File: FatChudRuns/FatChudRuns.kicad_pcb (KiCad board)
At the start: 2 copper layers, 0 parts

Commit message: selected rj45 w/ mag, fixed filtering for power, added snippets of layout recs
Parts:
- added J1: RJ45_Pulse_JXD6-0001NL, Connector_RJ:RJ45_Pulse_JXD6-0001NL_Horizontal, F.Cu at (-41.8, 67.0)
- added R1: 4.7k, Resistor_SMD:R_0603_1608Metric, F.Cu at (-10.6, 58.8)
- added R10: 2.2k, Resistor_SMD:R_0603_1608Metric, F.Cu at (-54.4, 90.2)
- added R11: 2.2k, Resistor_SMD:R_0603_1608Metric, F.Cu at (-54.4, 92.7)
- added R12: 2.2k, Resistor_SMD:R_0603_1608Metric, F.Cu at (-54.4, 95.2)
- added R13: 2.2k, Resistor_SMD:R_0603_1608Metric, F.Cu at (-54.4, 97.7)
- added R14: 2.2k, Resistor_SMD:R_0603_1608Metric, F.Cu at (-50.4, 77.7)
- added R15: 2.2k, Resistor_SMD:R_0603_1608Metric, F.Cu at (-50.4, 80.2)
- added R16: 2.2k, Resistor_SMD:R_0603_1608Metric, F.Cu at (-50.4, 82.7)
- added R17: 2.2k, Resistor_SMD:R_0603_1608Metric, F.Cu at (-50.4, 85.2)
- added R18: 2.2k, Resistor_SMD:R_0603_1608Metric, F.Cu at (-50.4, 87.7)
- added R19: 2.2k, Resistor_SMD:R_0603_1608Metric, F.Cu at (-50.4, 90.2)
- added R2: 4.7k, Resistor_SMD:R_0603_1608Metric, F.Cu at (-10.6, 61.3)
- added R20: 2.2k, Resistor_SMD:R_0603_1608Metric, F.Cu at (-50.4, 92.7)
- added R21: 2.2k, Resistor_SMD:R_0603_1608Metric, F.Cu at (-50.4, 95.2)
- added R22: 50, Resistor_SMD:R_0603_1608Metric, F.Cu at (-50.4, 97.7)
- added R23: 50, Resistor_SMD:R_0603_1608Metric, F.Cu at (-46.4, 77.7)
- added R24: 2.2k, Resistor_SMD:R_0603_1608Metric, F.Cu at (-46.4, 80.2)
- added R25: 50, Resistor_SMD:R_0603_1608Metric, F.Cu at (-46.4, 82.7)
- added R26: 50, Resistor_SMD:R_0603_1608Metric, F.Cu at (-46.4, 85.2)
- added R27: 2.2k, Resistor_SMD:R_0603_1608Metric, F.Cu at (-46.4, 87.7)
- added R28: 2.2k, Resistor_SMD:R_0603_1608Metric, F.Cu at (-46.4, 90.2)
- added R29: 2.2k, Resistor_SMD:R_0603_1608Metric, F.Cu at (-46.4, 92.7)
- added R3: 4.7k, Resistor_SMD:R_0603_1608Metric, F.Cu at (-10.6, 63.8)
- added R30: 2.2k, Resistor_SMD:R_0603_1608Metric, F.Cu at (-46.4, 95.2)
- added R31: 50, Resistor_SMD:R_0603_1608Metric, F.Cu at (-46.4, 97.7)
- added R32: 50, Resistor_SMD:R_0603_1608Metric, F.Cu at (-42.4, 77.7)
- added R33: 50, Resistor_SMD:R_0603_1608Metric, F.Cu at (-42.4, 80.2)
- added R34: 50, Resistor_SMD:R_0603_1608Metric, F.Cu at (-42.4, 82.7)
- added R35: 4.87k, Resistor_SMD:R_0603_1608Metric, F.Cu at (-42.4, 85.2)
- added R36: 2.2k, Resistor_SMD:R_0603_1608Metric, F.Cu at (-42.4, 87.7)
- added R37: 2.2k, Resistor_SMD:R_0603_1608Metric, F.Cu at (-42.4, 90.2)
- added R4: 4.7k, Resistor_SMD:R_0603_1608Metric, F.Cu at (-10.6, 66.3)
- added R5: 1.5k, Resistor_SMD:R_0603_1608Metric, F.Cu at (-54.4, 77.7)
- added R6: 2.2k, Resistor_SMD:R_0603_1608Metric, F.Cu at (-54.4, 80.2)
- added R7: 2.2k, Resistor_SMD:R_0603_1608Metric, F.Cu at (-54.4, 82.7)
- added R8: 0, Resistor_SMD:R_0603_1608Metric, F.Cu at (-54.4, 85.2)
- added R9: 0, Resistor_SMD:R_0603_1608Metric, F.Cu at (-54.4, 87.7)
- added U1: STM32F107RBTx, Package_QFP:LQFP-64_10x10mm_P0.5mm, F.Cu at (-19.8, 64.8)
- added U2: DP83848I, Package_QFP:LQFP-48_7x7mm_P0.5mm, F.Cu at (-34.7, 82.1)

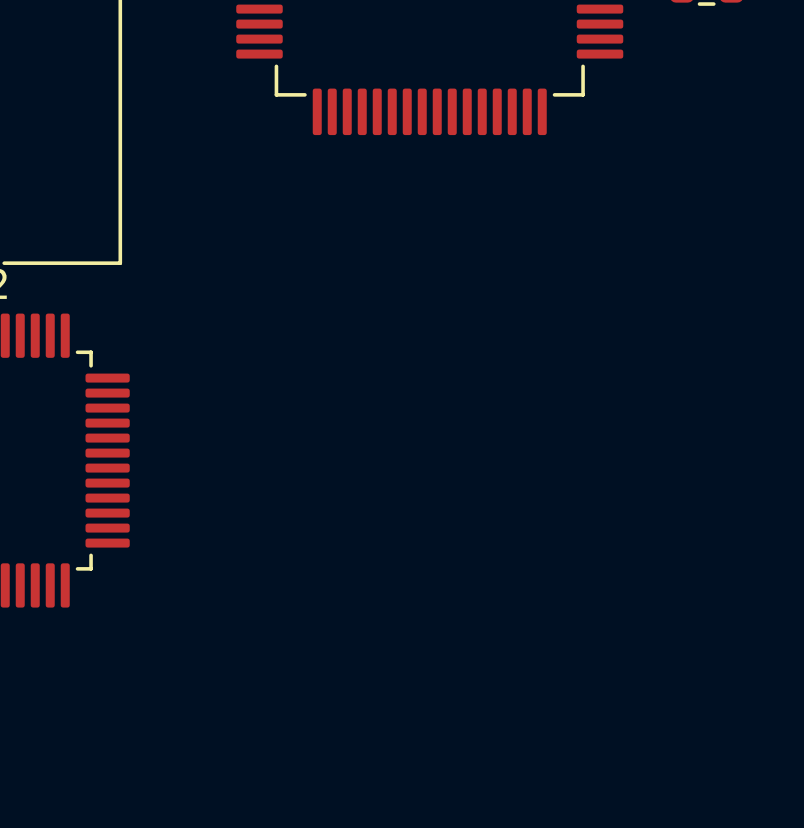
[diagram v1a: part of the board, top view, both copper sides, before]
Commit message: connected rj45 and leds and led strapping resistors
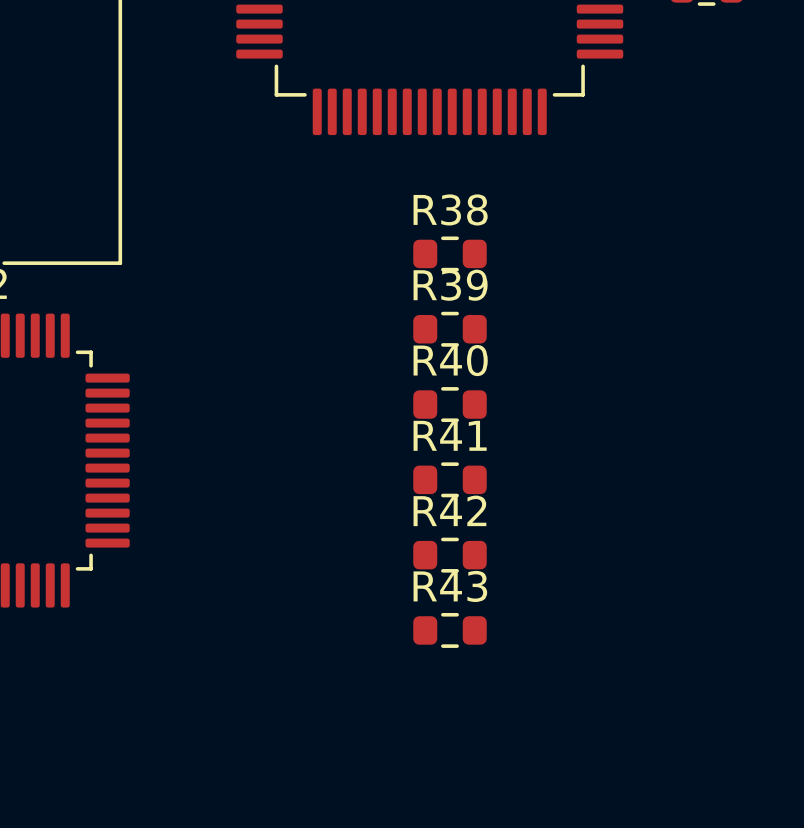
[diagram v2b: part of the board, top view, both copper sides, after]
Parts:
- added R38: 2.2k, Resistor_SMD:R_0603_1608Metric, F.Cu at (-19.2, 75.2)
- added R39: 110, Resistor_SMD:R_0603_1608Metric, F.Cu at (-19.2, 77.7)
- added R40: 2.2k, Resistor_SMD:R_0603_1608Metric, F.Cu at (-19.2, 80.2)
- added R41: 2.2k, Resistor_SMD:R_0603_1608Metric, F.Cu at (-19.2, 82.7)
- added R42: 2.2k, Resistor_SMD:R_0603_1608Metric, F.Cu at (-19.2, 85.2)
- added R43: 2.2k, Resistor_SMD:R_0603_1608Metric, F.Cu at (-19.2, 87.7)
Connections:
- J1 pad 1: unconnected-(J1-Pad1) -> /ETH_PHY/LED_LINK
- J1 pad 10: unconnected-(J1-Pad10) -> Net-(J1-Pad10)
- J1 pad 2: unconnected-(J1-Pad2) -> Net-(J1-Pad2)
- J1 pad 3: unconnected-(J1-TCT-Pad3) -> VP3V3
- J1 pad 4: unconnected-(J1-TD+-Pad4) -> /ETH_PHY/TD_P
- J1 pad 5: unconnected-(J1-TD--Pad5) -> /ETH_PHY/TD_N
- J1 pad 6: unconnected-(J1-RD+-Pad6) -> /ETH_PHY/RD_P
- J1 pad 7: unconnected-(J1-RD--Pad7) -> /ETH_PHY/RD_N
- J1 pad 8: unconnected-(J1-RCT-Pad8) -> VP3V3
- J1 pad 9: unconnected-(J1-Pad9) -> /ETH_PHY/LED_ACT
- J1 pad SH: unconnected-(J1-PadSH) -> CGND
- R31 pad 2: Net-(U2-RD+) -> /ETH_PHY/RD_P
- R32 pad 1: Net-(U2-RD-) -> /ETH_PHY/RD_N
- R33 pad 2: Net-(U2-TD+) -> /ETH_PHY/TD_P
- R34 pad 1: Net-(U2-TD-) -> /ETH_PHY/TD_N
- U2 pad 13: Net-(U2-RD-) -> /ETH_PHY/RD_N
- U2 pad 14: Net-(U2-RD+) -> /ETH_PHY/RD_P
- U2 pad 16: Net-(U2-TD-) -> /ETH_PHY/TD_N
- U2 pad 17: Net-(U2-TD+) -> /ETH_PHY/TD_P
- U2 pad 26: unconnected-(U2-AN_EN/LED_ACT/COL-Pad26) -> /ETH_PHY/LED_ACT
- U2 pad 27: unconnected-(U2-AN1/LED_SPEED-Pad27) -> /ETH_PHY/LED_SPEED
- U2 pad 28: unconnected-(U2-AN0/LED_LINK-Pad28) -> /ETH_PHY/LED_LINK

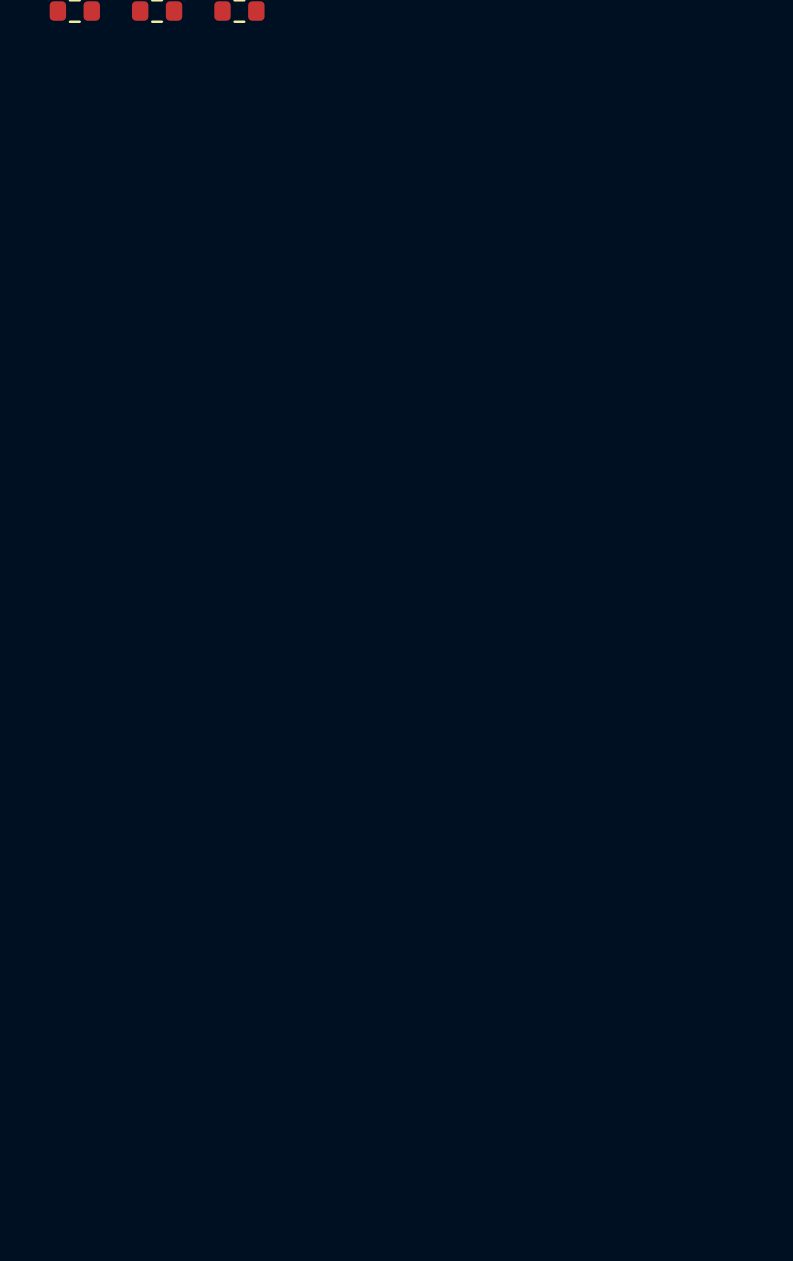
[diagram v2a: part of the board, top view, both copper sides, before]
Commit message: added connectors for gpio and jtag, need to verify orientation
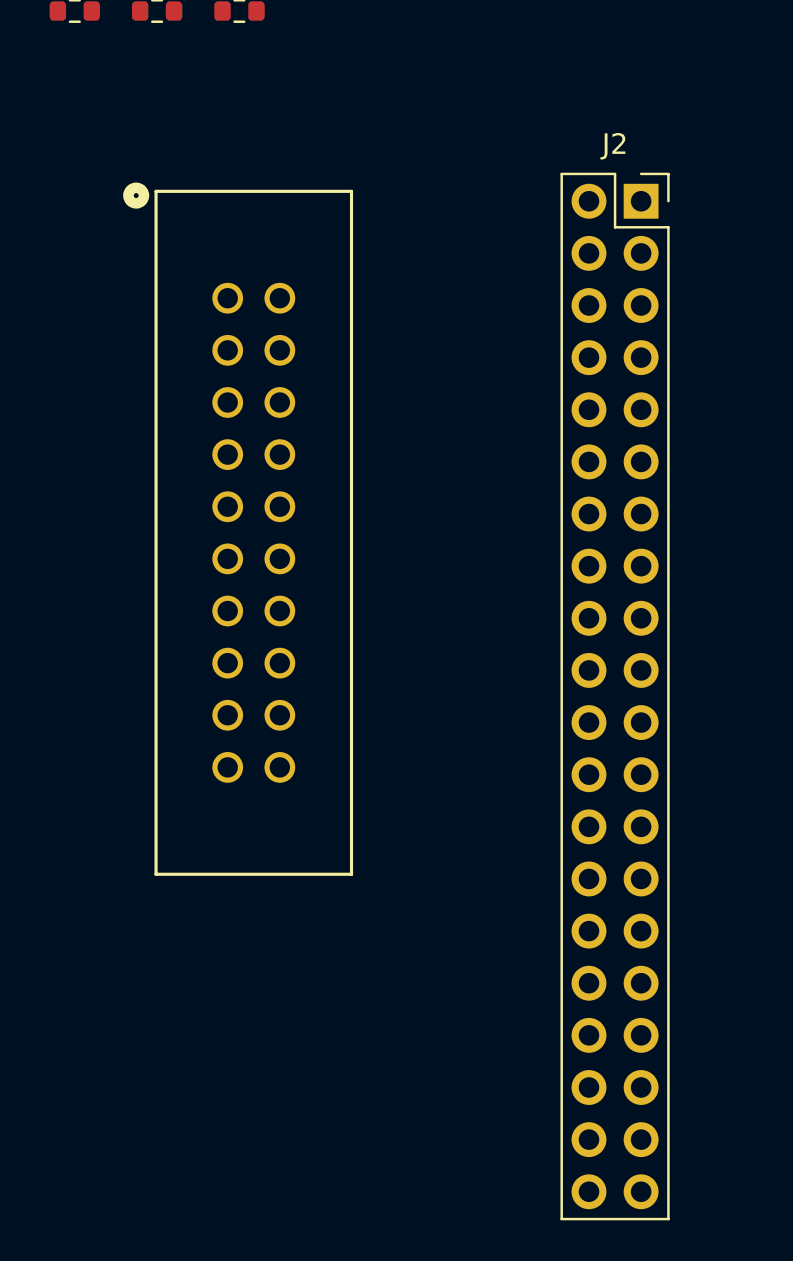
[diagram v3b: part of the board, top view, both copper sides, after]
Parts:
- added J2: Conn_02x20_Odd_Even, Connector_PinSocket_2.54mm:PinSocket_2x20_P2.54mm_Vertical, F.Cu at (-26.8, 107.0)
- added J3: TST-110-01-L-D, JTAG_20p_2.54mm:CONN20_TST_33P02X9P27_SAI, F.Cu at (-44.5, 111.7)
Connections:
- U1 pad 10: unconnected-(U1-PC2-Pad10) -> /MCU/PC2
- U1 pad 11: unconnected-(U1-PC3-Pad11) -> /MCU/PC3
- U1 pad 14: unconnected-(U1-PA0-Pad14) -> /MCU/PA0
- U1 pad 17: unconnected-(U1-PA3-Pad17) -> /MCU/PA3
- U1 pad 2: unconnected-(U1-PC13-Pad2) -> /MCU/PC13
- U1 pad 20: unconnected-(U1-PA4-Pad20) -> /MCU/PA4
- U1 pad 21: unconnected-(U1-PA5-Pad21) -> /MCU/PA5
- U1 pad 22: unconnected-(U1-PA6-Pad22) -> /MCU/PA6
- U1 pad 26: unconnected-(U1-PB0-Pad26) -> /MCU/PB0
- U1 pad 27: unconnected-(U1-PB1-Pad27) -> /MCU/PB1
- U1 pad 28: unconnected-(U1-PB2-Pad28) -> /MCU/PB2
- U1 pad 29: unconnected-(U1-PB10-Pad29) -> /MCU/PB10
- U1 pad 3: unconnected-(U1-PC14-Pad3) -> /MCU/PC14
- U1 pad 35: unconnected-(U1-PB14-Pad35) -> /MCU/PB14
- U1 pad 36: unconnected-(U1-PB15-Pad36) -> /MCU/PB15
- U1 pad 37: unconnected-(U1-PC6-Pad37) -> /MCU/PC6
- U1 pad 38: unconnected-(U1-PC7-Pad38) -> /MCU/PC7
- U1 pad 39: unconnected-(U1-PC8-Pad39) -> /MCU/PC8
- U1 pad 4: unconnected-(U1-PC15-Pad4) -> /MCU/PC15
- U1 pad 40: unconnected-(U1-PC9-Pad40) -> /MCU/PC9
- U1 pad 42: unconnected-(U1-PA9-Pad42) -> /MCU/PA9
- U1 pad 43: unconnected-(U1-PA10-Pad43) -> /MCU/PA10
- U1 pad 44: unconnected-(U1-PA11-Pad44) -> /MCU/PA11
- U1 pad 45: unconnected-(U1-PA12-Pad45) -> /MCU/PA12
- U1 pad 46: unconnected-(U1-PA13-Pad46) -> /MCU/PA13
- U1 pad 49: unconnected-(U1-PA14-Pad49) -> /MCU/PA14
- U1 pad 5: unconnected-(U1-PD0-Pad5) -> /MCU/PD0
- U1 pad 50: unconnected-(U1-PA15-Pad50) -> /MCU/PA15
- U1 pad 51: unconnected-(U1-PC10-Pad51) -> /MCU/PC10
- U1 pad 52: unconnected-(U1-PC11-Pad52) -> /MCU/PC11
- U1 pad 53: unconnected-(U1-PC12-Pad53) -> /MCU/PC12
- U1 pad 54: unconnected-(U1-PD2-Pad54) -> /MCU/PD2
- U1 pad 55: unconnected-(U1-PB3-Pad55) -> /MCU/PB3
- U1 pad 56: unconnected-(U1-PB4-Pad56) -> /MCU/PB4
- U1 pad 57: unconnected-(U1-PB5-Pad57) -> /MCU/PB5
- U1 pad 58: unconnected-(U1-PB6-Pad58) -> /MCU/PB6
- U1 pad 59: unconnected-(U1-PB7-Pad59) -> /MCU/PB7
- U1 pad 6: unconnected-(U1-PD1-Pad6) -> /MCU/PD1
- U1 pad 61: unconnected-(U1-PB8-Pad61) -> /MCU/PB8
- U1 pad 62: unconnected-(U1-PB9-Pad62) -> /MCU/PB9
- U1 pad 8: unconnected-(U1-PC0-Pad8) -> /MCU/PC0

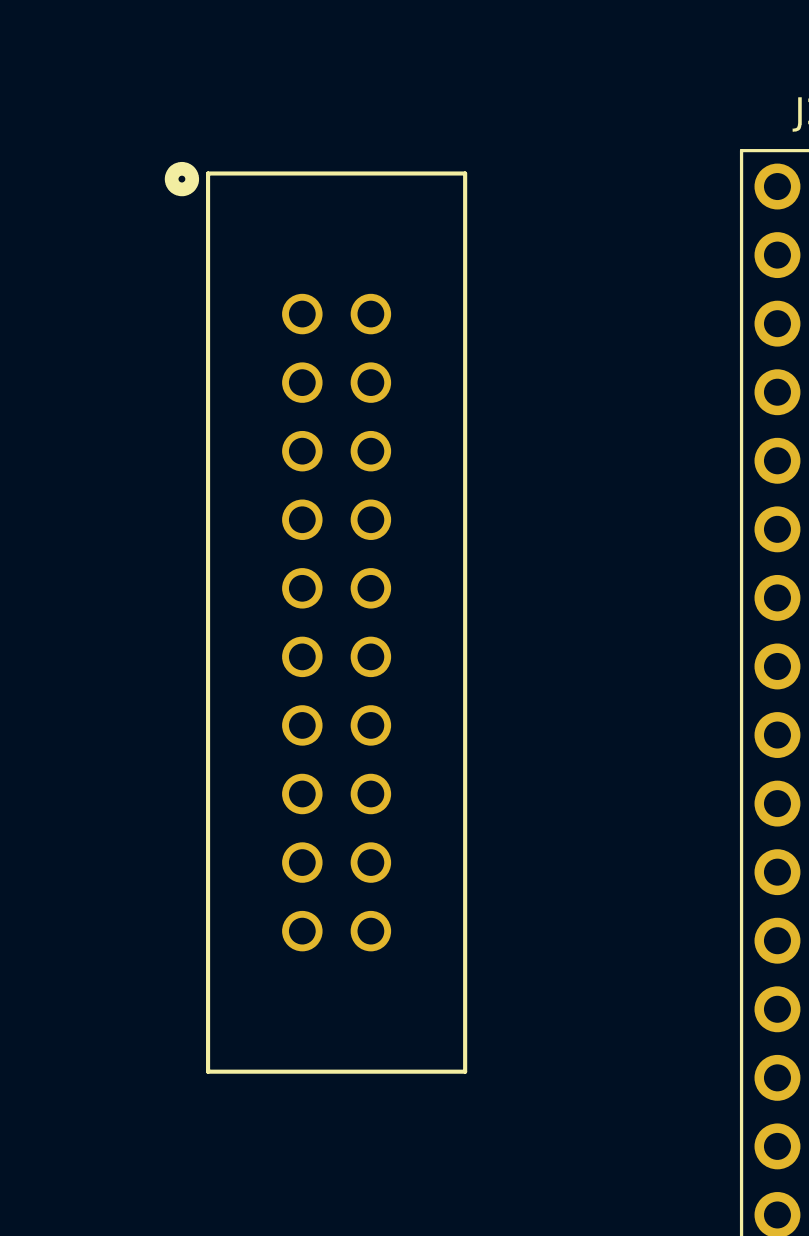
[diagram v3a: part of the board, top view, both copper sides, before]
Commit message: added debugger and nucleo ref sch
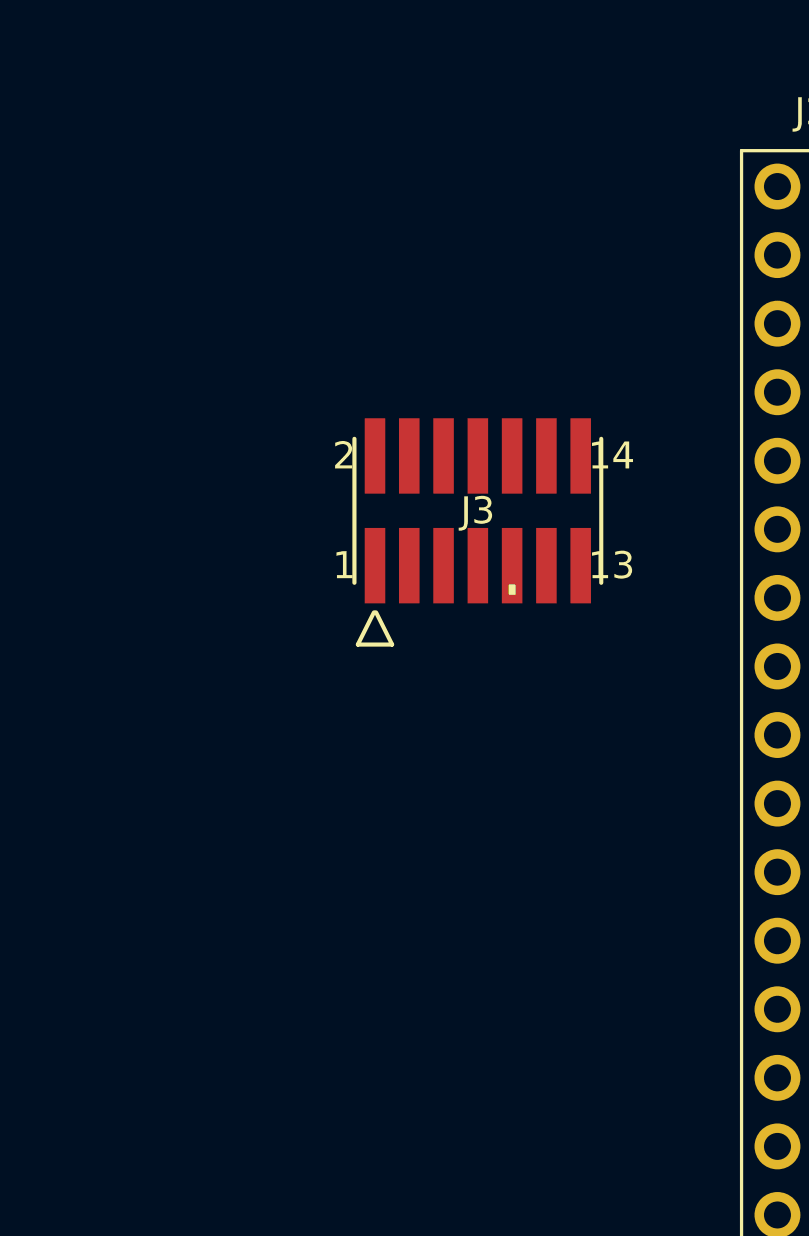
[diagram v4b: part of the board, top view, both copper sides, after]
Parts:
- J3: value TST-110-01-L-D -> FTSH-107-01-L-DV-K-P; footprint JTAG_20p_2.54mm:CONN20_TST_33P02X9P27_SAI -> CON14_2X7_DUK_FTSH_SAI:CON14_2X7_DUK_FTSH_SAI
- moved J3 8.30 mm to (-40.5, 119.0), turned to 0 degrees
